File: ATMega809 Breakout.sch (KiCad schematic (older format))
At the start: 50 parts, among them J1 USB_B_Micro, J2 Conn_01x05, J3 Conn_01x20, J4 Conn_01x12, J5 UPDI, Q1 PJA3438-AU, Q2 PJA3438-AU, Q3 PJA3438-AU, Q4 PJA3438-AU, Q5 PJA3438-AU, SW1 RESET, U1 NCP1117-ADJ_SOT223, U2 ATMEGA809-AF

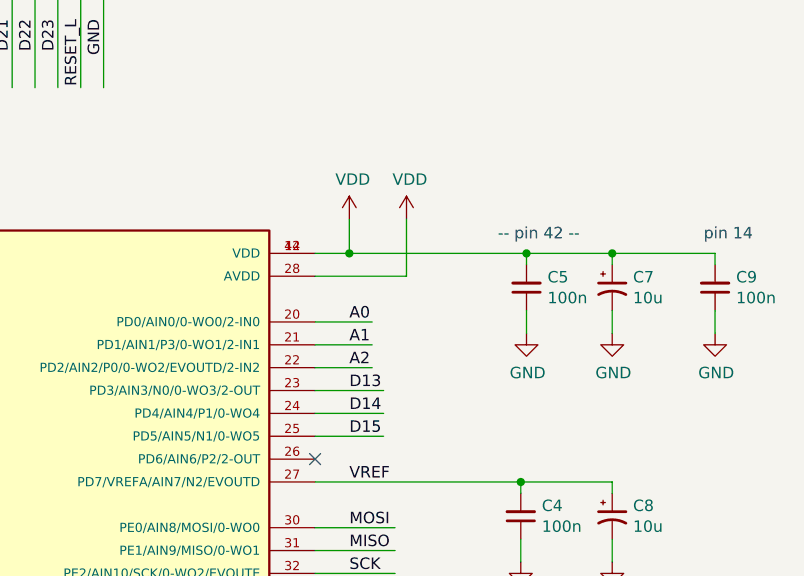
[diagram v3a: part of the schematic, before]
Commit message: Add decoupling cap C10 for AVDD pin of MCU.
Add 100nF stabilizing ballast to AVDD input (MCU pin 28).
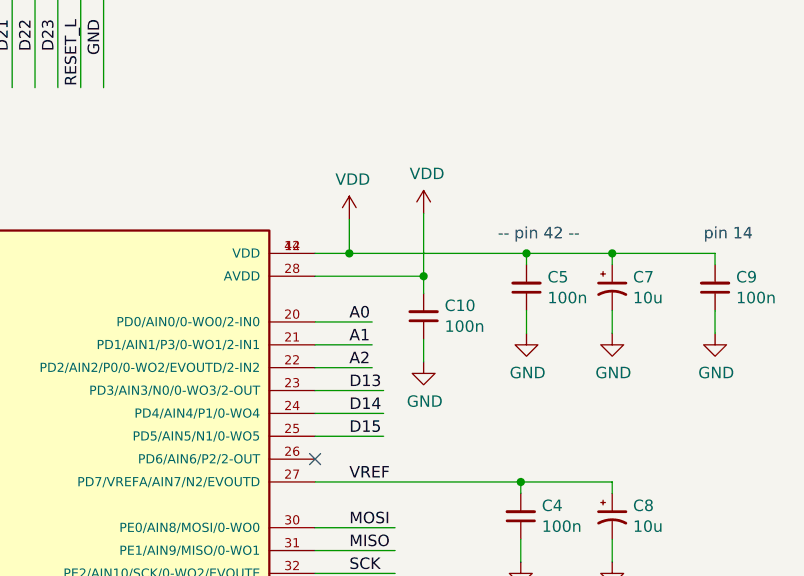
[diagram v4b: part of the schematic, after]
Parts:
- added C10: 100n, Capacitor_SMD:C_0603_1608Metric, symbol Device:C_Small
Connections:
- wire segments 209 -> 211
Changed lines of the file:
@@
 Text Notes 9850 3250 0    50   ~ 0
 -- pin 42 --
-Wire Wire Line
-	9050 3400 9450 3400
-Wire Wire Line
-	9450 3400 9450 3150
 $Comp
 L power:VDD #PWR019
 U 1 1 625D2F02
-P 9450 3150
-F 0 "#PWR019" H 9450 3000 50  0001 C CNN
-F 1 "VDD" H 9465 3323 50  0000 C CNN
-F 2 "" H 9450 3150 50  0001 C CNN
-F 3 "" H 9450 3150 50  0001 C CNN
-	1    9450 3150
+P 9525 3125
+F 0 "#PWR019" H 9525 2975 50  0001 C CNN
+F 1 "VDD" H 9540 3298 50  0000 C CNN
+F 2 "" H 9525 3125 50  0001 C CNN
+F 3 "" H 9525 3125 50  0001 C CNN
+	1    9525 3125
 	1    0    0    -1
 $EndComp
@@
 Text GLabel 9550 1300 0    50   BiDi ~ 0
 UPDI
+$Comp
+L Device:C_Small C10
+U 1 1 62F5FF22
+P 9525 3575
+F 0 "C10" H 9433 3529 50  0000 R CNN
+F 1 "100n" H 9433 3620 50  0000 R CNN
+F 2 "Capacitor_SMD:C_0603_1608Metric" H 9525 3575 50  0001 C CNN
+F 3 "https://datasheets.kyocera-avx.com/X7RDielectric.pdf" H 9525 3575 50  0001 C CNN
+F 4 "06036C104JAT2A" H 9525 3575 50  0001 C CNN "MPN"
+F 5 "KYOCERA" H 9525 3575 50  0001 C CNN "MANUFACTURER"
+	1    9525 3575
+	-1   0    0    1
+$EndComp
+Wire Wire Line
+	9525 3400 9525 3125
+Wire Wire Line
+	9525 3475 9525 3400
+Connection ~ 9525 3400
+Wire Wire Line
+	9050 3400 9525 3400
+$Comp
+L power:GND #PWR030
+U 1 1 62F7AEA6
+P 9525 3775
+F 0 "#PWR030" H 9525 3525 50  0001 C CNN
+F 1 "GND" H 9530 3602 50  0000 C CNN
+F 2 "" H 9525 3775 50  0001 C CNN
+F 3 "" H 9525 3775 50  0001 C CNN
+	1    9525 3775
+	1    0    0    -1
+$EndComp
+Wire Wire Line
+	9525 3775 9525 3675
 $EndSCHEMATC

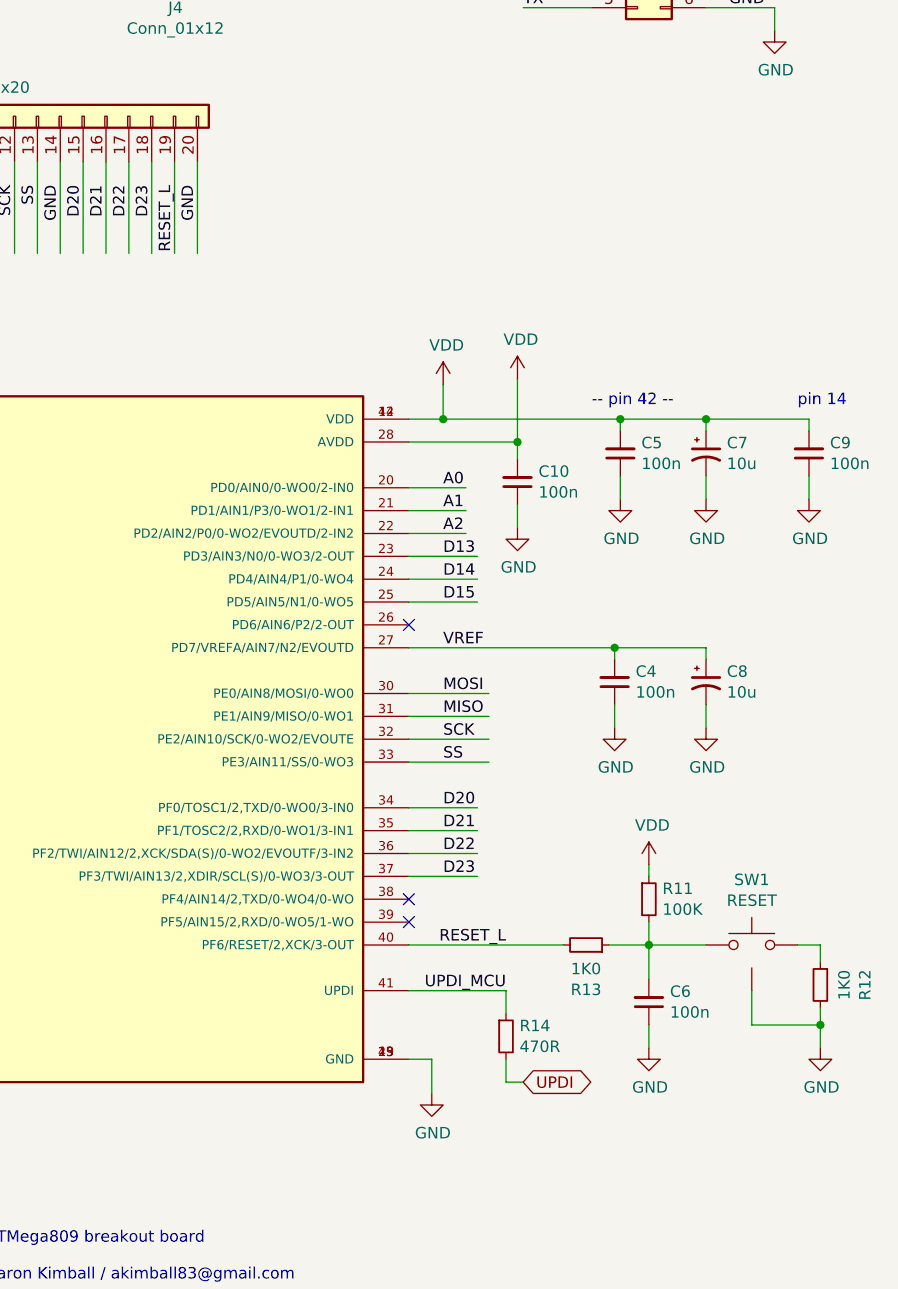
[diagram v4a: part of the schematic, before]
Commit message: Tweak RST protection resistor placement.
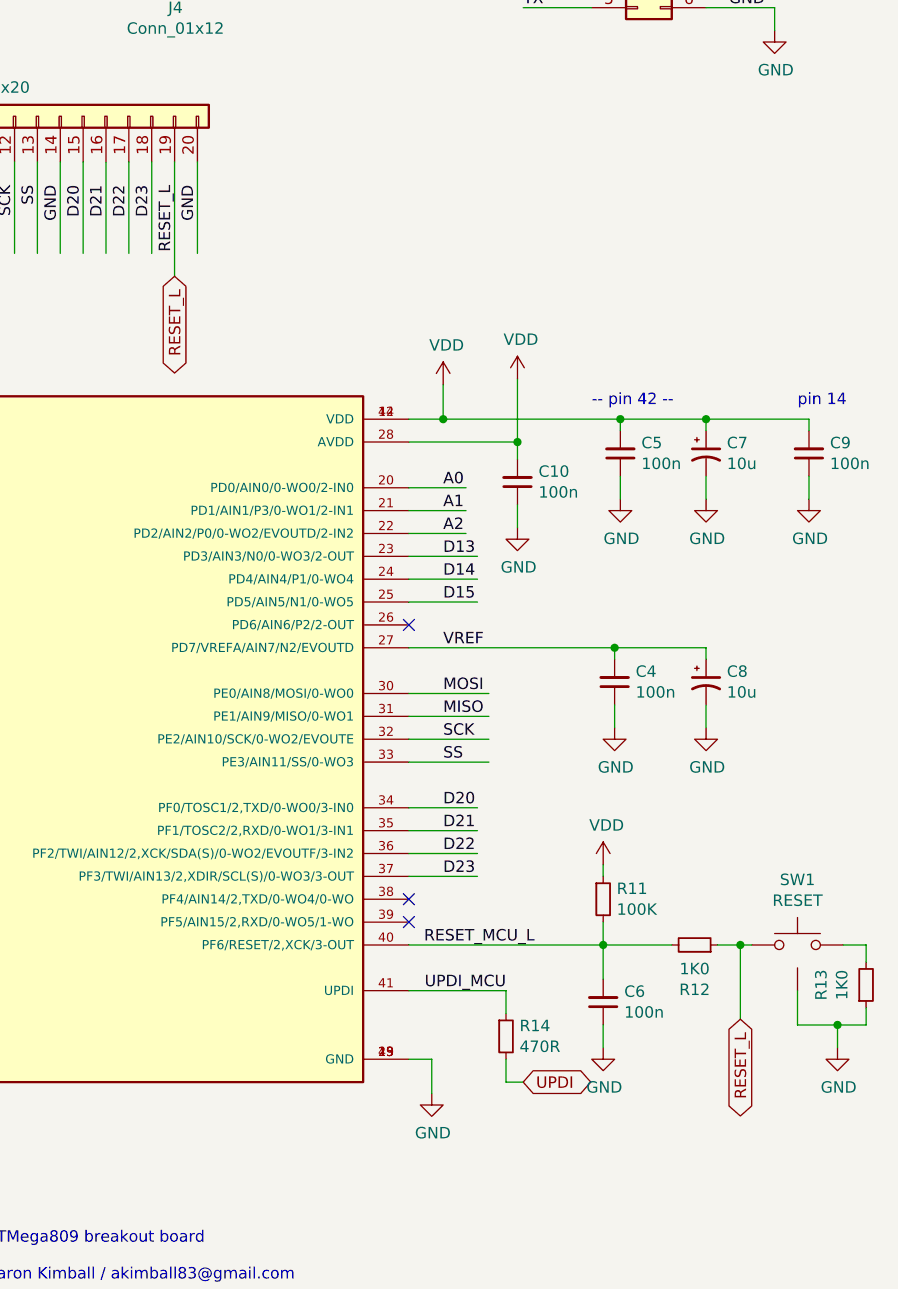
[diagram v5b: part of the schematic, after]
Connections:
- net labels added: RESET_MCU_L
- wire segments 211 -> 214
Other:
- moved on the sheet: C6, R11, R12, SW1
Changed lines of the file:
@@
 Text Label 9475 5800 2    50   ~ 0
 UPDI_MCU
-Text Label 9475 5600 2    50   ~ 0
-RESET_L
+Text Label 9600 5600 2    50   ~ 0
+RESET_MCU_L
 $Comp
 L Device:R_Small R11
 U 1 1 625C66FF
-P 10100 5400
-F 0 "R11" H 10159 5446 50  0000 L CNN
-F 1 "100K" H 10159 5355 50  0000 L CNN
-F 2 "Resistor_SMD:R_0603_1608Metric" H 10100 5400 50  0001 C CNN
-F 3 "~" H 10100 5400 50  0001 C CNN
-F 4 "RC0603FR-07100KL" H 10100 5400 50  0001 C CNN "MPN"
-F 5 "YAEGO" H 10100 5400 50  0001 C CNN "MANUFACTURER"
-	1    10100 5400
+P 9900 5400
+F 0 "R11" H 9959 5446 50  0000 L CNN
+F 1 "100K" H 9959 5355 50  0000 L CNN
+F 2 "Resistor_SMD:R_0603_1608Metric" H 9900 5400 50  0001 C CNN
+F 3 "~" H 9900 5400 50  0001 C CNN
+F 4 "RC0603FR-07100KL" H 9900 5400 50  0001 C CNN "MPN"
+F 5 "YAEGO" H 9900 5400 50  0001 C CNN "MANUFACTURER"
+	1    9900 5400
 	1    0    0    -1
 $EndComp
@@
 L power:VDD #PWR022
 U 1 1 625C6C2F
-P 10100 5250
-F 0 "#PWR022" H 10100 5100 50  0001 C CNN
-F 1 "VDD" H 10115 5423 50  0000 C CNN
-F 2 "" H 10100 5250 50  0001 C CNN
-F 3 "" H 10100 5250 50  0001 C CNN
-	1    10100 5250
-	1    0    0    -1
-$EndComp
-Wire Wire Line
-	10100 5250 10100 5300
+P 9900 5250
+F 0 "#PWR022" H 9900 5100 50  0001 C CNN
+F 1 "VDD" H 9915 5423 50  0000 C CNN
+F 2 "" H 9900 5250 50  0001 C CNN
+F 3 "" H 9900 5250 50  0001 C CNN
+	1    9900 5250
+	1    0    0    -1
+$EndComp
+Wire Wire Line
+	9900 5250 9900 5300
 Text Label 9200 4300 0    50   ~ 0
 VREF
 Wire Wire Line
-	10100 5600 10100 5500
+	9900 5600 9900 5500
 $Comp
 L Device:C_Small C5
@@
 L Device:C_Small C6
 U 1 1 625D7A5C
-P 10100 5850
-F 0 "C6" H 10008 5804 50  0000 R CNN
-F 1 "100n" H 10008 5895 50  0000 R CNN
-F 2 "Capacitor_SMD:C_0603_1608Metric" H 10100 5850 50  0001 C CNN
-F 3 "https://datasheets.kyocera-avx.com/X7RDielectric.pdf" H 10100 5850 50  0001 C CNN
-F 4 "06036C104JAT2A" H 10100 5850 50  0001 C CNN "MPN"
-F 5 "KYOCERA" H 10100 5850 50  0001 C CNN "MANUFACTURER"
-	1    10100 5850
+P 9900 5850
+F 0 "C6" H 9808 5804 50  0000 R CNN
+F 1 "100n" H 9808 5895 50  0000 R CNN
+F 2 "Capacitor_SMD:C_0603_1608Metric" H 9900 5850 50  0001 C CNN
+F 3 "https://datasheets.kyocera-avx.com/X7RDielectric.pdf" H 9900 5850 50  0001 C CNN
+F 4 "06036C104JAT2A" H 9900 5850 50  0001 C CNN "MPN"
+F 5 "KYOCERA" H 9900 5850 50  0001 C CNN "MANUFACTURER"
+	1    9900 5850
 	-1   0    0    1
 $EndComp
 Wire Wire Line
-	10100 5750 10100 5600
-Connection ~ 10100 5600
+	9900 5750 9900 5600
+Connection ~ 9900 5600
 $Comp
 L power:GND #PWR023
 U 1 1 625D8641
-P 10100 6050
-F 0 "#PWR023" H 10100 5800 50  0001 C CNN
-F 1 "GND" H 10105 5877 50  0000 C CNN
-F 2 "" H 10100 6050 50  0001 C CNN
-F 3 "" H 10100 6050 50  0001 C CNN
-	1    10100 6050
-	1    0    0    -1
-$EndComp
-Wire Wire Line
-	10100 6050 10100 5950
+P 9900 6050
+F 0 "#PWR023" H 9900 5800 50  0001 C CNN
+F 1 "GND" H 9905 5877 50  0000 C CNN
+F 2 "" H 9900 6050 50  0001 C CNN
+F 3 "" H 9900 6050 50  0001 C CNN
+	1    9900 6050
+	1    0    0    -1
+$EndComp
+Wire Wire Line
+	9900 6050 9900 5950
 $Comp
 L Aaron-Symbols:SW_Push_GND SW1
 U 1 1 625D9E24
-P 10550 5600
-F 0 "SW1" H 10550 5885 50  0000 C CNN
-F 1 "RESET" H 10550 5794 50  0000 C CNN
-F 2 "aaron-imported-parts:PTS820_J25K_SMTR_LFS" H 10550 5800 50  0001 C CNN
-F 3 "https://www.ckswitches.com/media/1474/pts820.pdf" H 10550 5800 50  0001 C CNN
-F 4 "PTS820 J25K SMTR LFS" H 10550 5600 50  0001 C CNN "MPN"
-F 5 "C&K" H 10550 5600 50  0001 C CNN "MANUFACTURER"
-	1    10550 5600
-	1    0    0    -1
-$EndComp
-Wire Wire Line
-	10350 5600 10100 5600
+P 10750 5600
+F 0 "SW1" H 10750 5885 50  0000 C CNN
+F 1 "RESET" H 10750 5794 50  0000 C CNN
+F 2 "aaron-imported-parts:PTS820_J25K_SMTR_LFS" H 10750 5800 50  0001 C CNN
+F 3 "https://www.ckswitches.com/media/1474/pts820.pdf" H 10750 5800 50  0001 C CNN
+F 4 "PTS820 J25K SMTR LFS" H 10750 5600 50  0001 C CNN "MPN"
+F 5 "C&K" H 10750 5600 50  0001 C CNN "MANUFACTURER"
+	1    10750 5600
+	1    0    0    -1
+$EndComp
 $Comp
 L power:GND #PWR029
 U 1 1 625DACF2
-P 10850 6050
-F 0 "#PWR029" H 10850 5800 50  0001 C CNN
-F 1 "GND" H 10855 5877 50  0000 C CNN
-F 2 "" H 10850 6050 50  0001 C CNN
-F 3 "" H 10850 6050 50  0001 C CNN
-	1    10850 6050
-	1    0    0    -1
-$EndComp
-Wire Wire Line
-	10750 5600 10850 5600
+P 10925 6050
+F 0 "#PWR029" H 10925 5800 50  0001 C CNN
+F 1 "GND" H 10930 5877 50  0000 C CNN
+F 2 "" H 10925 6050 50  0001 C CNN
+F 3 "" H 10925 6050 50  0001 C CNN
+	1    10925 6050
+	1    0    0    -1
+$EndComp
+Wire Wire Line
+	10950 5600 11050 5600
 Wire Wire Line
 	4650 3600 4250 3600
@@
 GPIO LED
 Wire Wire Line
-	10550 5950 10850 5950
-Wire Wire Line
-	10850 5950 10850 6050
+	10925 5950 10925 6050
 $Comp
 L Connector_Generic:Conn_01x05 J2
@@
 Wire Wire Line
 	6425 2575 6425 2175
-Wire Wire Line
-	8025 2175 8025 2575
 Text Label 7425 2275 3    50   ~ 0
 SS
@@
 L Device:R_Small R12
 U 1 1 62DCA660
-P 10850 5775
-F 0 "R12" V 10654 5775 50  0000 C CNN
-F 1 "1K0" V 10745 5775 50  0000 C CNN
-F 2 "Resistor_SMD:R_0603_1608Metric" H 10850 5775 50  0001 C CNN
-F 3 "~" H 10850 5775 50  0001 C CNN
-F 4 "RC0603FR-071KL" H 10850 5775 50  0001 C CNN "MPN"
-F 5 "YAEGO" H 10850 5775 50  0001 C CNN "MANUFACTURER"
-	1    10850 5775
-	-1   0    0    -1
-$EndComp
-Wire Wire Line
-	10550 5800 10550 5950
-Wire Wire Line
-	10850 5875 10850 5950
-Connection ~ 10850 5950
-Wire Wire Line
-	10850 5675 10850 5600
-$Comp
-L Device:R_Small R13
-U 1 1 62E3EAED
-P 9825 5600
-F 0 "R13" V 9629 5600 50  0000 C CNN
-F 1 "1K0" V 9720 5600 50  0000 C CNN
-F 2 "Resistor_SMD:R_0603_1608Metric" H 9825 5600 50  0001 C CNN
-F 3 "~" H 9825 5600 50  0001 C CNN
-F 4 "RC0603FR-071KL" H 9825 5600 50  0001 C CNN "MPN"
-F 5 "YAEGO" H 9825 5600 50  0001 C CNN "MANUFACTURER"
-	1    9825 5600
+P 10300 5600
+F 0 "R12" V 10104 5600 50  0000 C CNN
+F 1 "1K0" V 10195 5600 50  0000 C CNN
+F 2 "Resistor_SMD:R_0603_1608Metric" H 10300 5600 50  0001 C CNN
+F 3 "~" H 10300 5600 50  0001 C CNN
+F 4 "RC0603FR-071KL" H 10300 5600 50  0001 C CNN "MPN"
+F 5 "YAEGO" H 10300 5600 50  0001 C CNN "MANUFACTURER"
+	1    10300 5600
 	0    1    -1   0
 $EndComp
 Wire Wire Line
-	9925 5600 10100 5600
-Wire Wire Line
-	9725 5600 9050 5600
+	10750 5800 10750 5950
 $Comp
 L Device:R_Small R14
@@
 Wire Wire Line
 	9525 3775 9525 3675
+Wire Wire Line
+	9050 5600 9900 5600
+Wire Wire Line
+	10750 5950 10925 5950
+Wire Wire Line
+	9900 5600 10200 5600
+Wire Wire Line
+	10925 5950 11050 5950
+Connection ~ 10925 5950
+Text GLabel 10500 5925 3    50   BiDi ~ 0
+RESET_L
+Wire Wire Line
+	10400 5600 10500 5600
+Wire Wire Line
+	10500 5925 10500 5600
+Connection ~ 10500 5600
+Wire Wire Line
+	10500 5600 10550 5600
+Text GLabel 8025 2675 3    50   BiDi ~ 0
+RESET_L
+Wire Wire Line
+	8025 2175 8025 2675
+$Comp
+L Device:R_Small R13
+U 1 1 6309FDF0
+P 11050 5775
+F 0 "R13" V 10854 5775 50  0000 C CNN
+F 1 "1K0" V 10945 5775 50  0000 C CNN
+F 2 "Resistor_SMD:R_0603_1608Metric" H 11050 5775 50  0001 C CNN
+F 3 "~" H 11050 5775 50  0001 C CNN
+F 4 "RC0603FR-071KL" H 11050 5775 50  0001 C CNN "MPN"
+F 5 "YAEGO" H 11050 5775 50  0001 C CNN "MANUFACTURER"
+	1    11050 5775
+	1    0    0    1
+$EndComp
+Wire Wire Line
+	11050 5675 11050 5600
+Wire Wire Line
+	11050 5875 11050 5950
 $EndSCHEMATC

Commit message: v1.0 Release to manufacturing
* Add BOM data to KiCAD and export to Excel.
* Elaborate on fab notes TXT file.
* Generate gerber files, schematic pdf, drill file, placement file for mfr.
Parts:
- C1, C3, C7, C8: Description (none) -> 10uF 0805 X5R or X7R ceramic capacitor; 20mOhm < ESR < 10 O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
- C10, C2, C4, C5, C6, C9: Description (none) -> 100nF 0603 X7R ceramic capacitor; 20mOhm < ESR < 10 Ohm
- D1, D2: Description (none) -> Schottky diode; V_R >= 30V; I_fwd >= 1A; 250mA < V_fwd < 34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
- D3, D4: Description (none) -> Red chip LED; 0603; Vfwd = 1.8--2.0V, I_test = 2mA; >= 2mcd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
- J1: Description (none) -> USB Micro-B receptacle; SMT; no flanges; board-edge
- J2: Description (none) -> Cuttable male pin THT header strip (5 pins), 0.1\"/2.54mm p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
- J3: Description (none) -> Cuttable male pin THT header strip (20 pins), 0.1\"/2.54mm 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
- J4: Description (none) -> Cuttable male pin THT header strip (12 pins), 0.1\"/2.54mm 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
- J5: Description (none) -> Male pin THT header 2-row strip (2x3 pins), 0.1\"/2.54mm pi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
- JP1: Description (none) -> Cuttable male pin THT header strip (2 pins), 0.1\"/2.54mm p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
- Q1, Q2, Q3, Q4, Q5: Description (none) -> N-MOSFET; SOT-23; I_D >= 500mA; max V_DS >= 50V; max V_GS +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
- R1, R11, R2: Description (none) -> 100K 0603 resistor; +/-1%; 1/10W
- R10, R14, R9: Description (none) -> 470R 0603 resistor; +/-1%; 1/10W
- R12, R13, R3: Description (none) -> 1K 0603 resistor; +/-1%; 1/10W
- R4: Description (none) -> 560R 0603 resistor; +/-1%; 1/10W
- R5, R6: Description (none) -> 4K7 0603 resistor; +/-1%; 1/10W
- R7: Description (none) -> 120R 0603 resistor; +/-1%; 1/10W
- R8: Description (none) -> 390R 0603 resistor; +/-1%; 1/10W
- SW1: Description (none) -> Tactile momentary SPST (normally-open) switch/button; groun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
- U1: Description (none) -> Adjustable linear regulator; SOT223 package; dropout voltag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
- U2: Description (none) -> Critical component. ATMEGA809-AU also OK. -AFR and -AUR (ta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
